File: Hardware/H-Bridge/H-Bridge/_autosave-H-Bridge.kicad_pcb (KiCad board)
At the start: 2 copper layers, 74.4 x 46 mm, 28 parts, among them Q1 SI4156DY, Q2 SI4156DY, Q3 SI4156DY, Q4 SI4156DY, U1 IRS2005S, U2 IRS2005S, U3 Teensy4.1_DEV-16771, U4 OKI

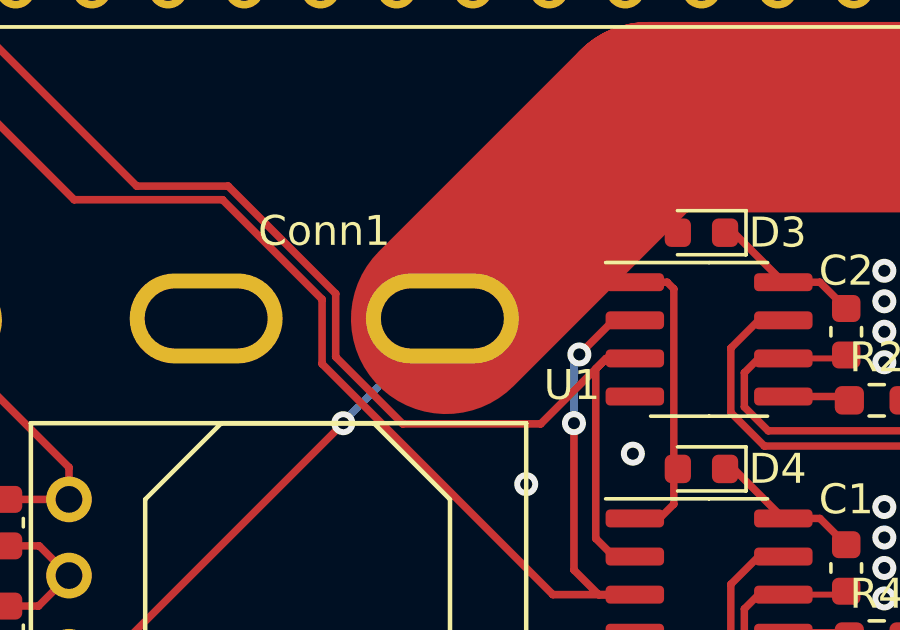
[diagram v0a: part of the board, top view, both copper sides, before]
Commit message: Initial PCB Layout with Revised H-Bridges
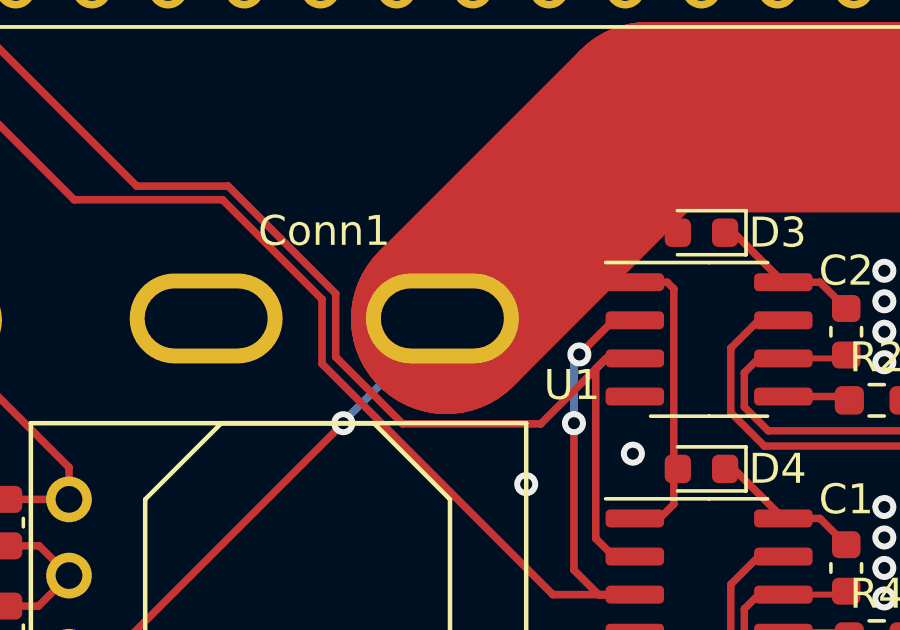
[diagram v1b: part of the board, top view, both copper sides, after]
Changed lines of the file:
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@@
   (gr_line (start 127.254 46.500051) (end 57.912 46.482) (layer "Edge.Cuts") (width 0.1))
   (gr_arc (start 57.912 92.456) (mid 56.115949 91.712051) (end 55.372 89.916) (layer "Edge.Cuts") (width 0.1))
-  (dimension (type aligned) (layer "F.Cu")
-    (pts (xy 97.172 77.63) (xy 97.172 80.104))
-    (height 0)
-    (gr_text "97.4016 mils" (at 95.372 78.867 90) (layer "F.Cu")
-      (effects (font (size 1.5 1.5) (thickness 0.3)))
-    )
-    (format (units 3) (units_format 1) (precision 4))
-    (style (thickness 0.2) (arrow_length 1.27) (text_position_mode 0) (extension_height 0.58642) (extension_offset 0.5) keep_text_aligned)
-  )
-  (dimension (type aligned) (layer "F.Cu")
-    (pts (xy 108.348 80.104) (xy 111.76 80.104))
-    (height -1.237)
-    (gr_text "134.3307 mils" (at 110.054 77.067) (layer "F.Cu")
-      (effects (font (size 1.5 1.5) (thickness 0.3)))
-    )
-    (format (units 3) (units_format 1) (precision 4))
-    (style (thickness 0.2) (arrow_length 1.27) (text_position_mode 0) (extension_height 0.58642) (extension_offset 0.5) keep_text_aligned)
-  )
   (segment (start 102.2115 71.374) (end 102.2115 72.9865) (width 0.25) (layer "F.Cu") (net 1))
   (segment (start 70.104 81.814) (end 71.146 81.814) (width 0.25) (layer "F.Cu") (net 1))
@@
   (segment (start 87.8612 77.7468) (end 83.258424 77.7468) (width 0.254) (layer "F.Cu") (net 13))
   (segment (start 70.13 85.344) (end 70.104 85.37) (width 0.25) (layer "F.Cu") (net 63))
+  (segment (start 84.709 74.2448) (end 84.9633 73.9905) (width 6.35) (layer "F.Cu") (net 63))
   (segment (start 92.297 80.423) (end 92.297 73.247) (width 0.25) (layer "F.Cu") (net 63))
   (segment (start 90.997 80.899) (end 91.821 80.899) (width 0.25) (layer "F.Cu") (net 63))
